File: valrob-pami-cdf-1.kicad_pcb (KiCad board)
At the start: 4 copper layers, 58 x 50 mm, 138 parts, among them J1 Conn_01x04, J2 USB_C_Receptacle_USB2.0_14P, J3 Conn_01x02, J4 Conn_01x04_Pin, J5 Conn_01x06, M1 Motor_Servo, M2 Stepper_Motor_bipolar, M3 Stepper_Motor_bipolar, Q1 Q_NMOS, Q2 Q_NMOS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

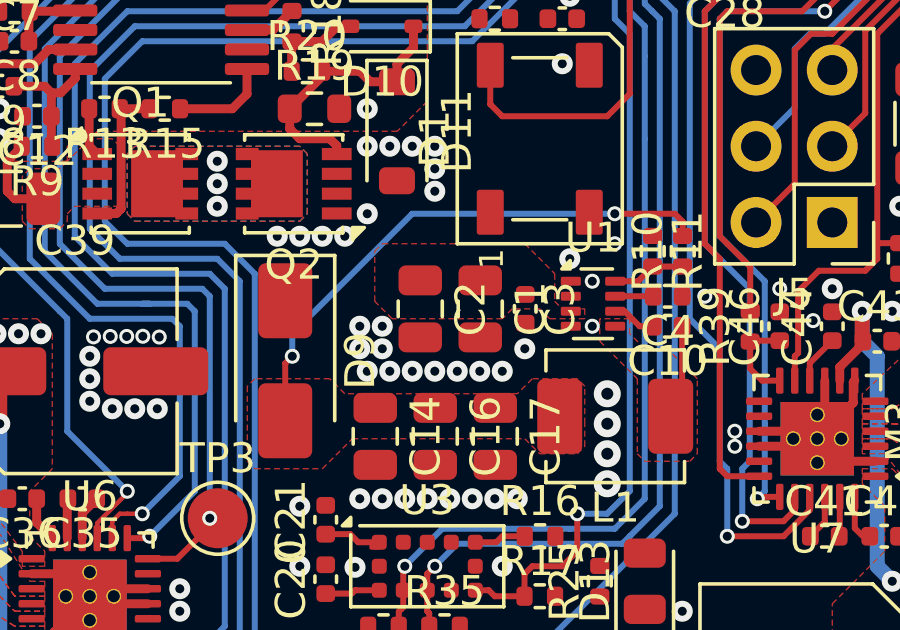
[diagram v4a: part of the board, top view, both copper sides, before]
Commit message: pcb: add +BATT routing
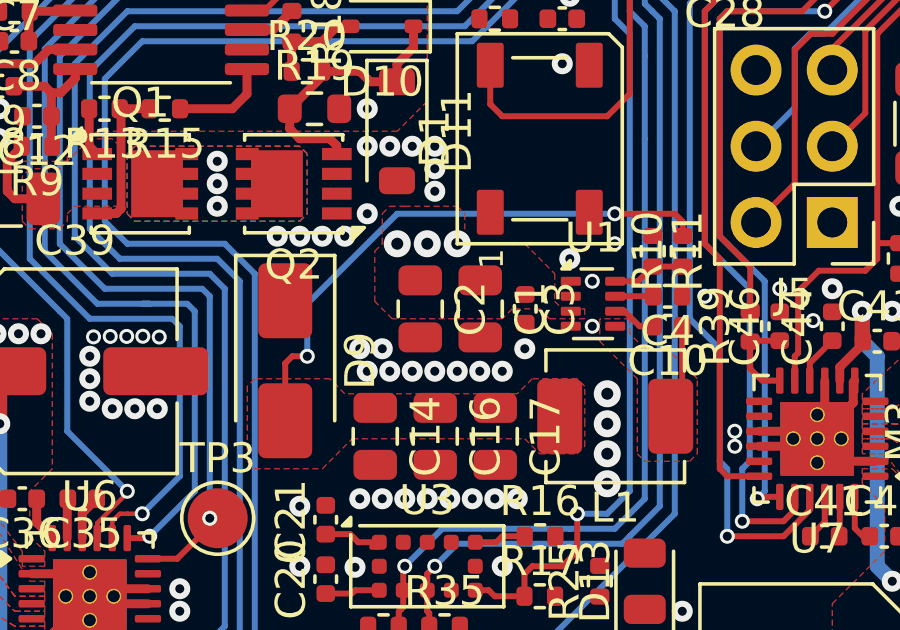
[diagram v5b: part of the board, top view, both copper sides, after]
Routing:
- net +BATT: track 55.5 -> 140.5 mm, vias 14 -> 17
- net +5V: track 18.3 -> 18.9 mm
- net GND: vias 113 -> 111
- added copper zone on In2.Cu, net +BATT
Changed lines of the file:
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@@
 	)
 	(via
-		(at 153.25 105.75)
-		(size 0.7)
-		(drill 0.3)
-		(layers "F.Cu" "B.Cu")
-		(free yes)
-		(net 4)
-	)
-	(via
 		(at 155.75 101.25)
 		(size 0.7)
@@
 	)
 	(via
-		(at 154 105.75)
-		(size 0.7)
-		(drill 0.3)
-		(layers "F.Cu" "B.Cu")
-		(free yes)
-		(net 4)
-	)
-	(via
 		(at 146.5 108.5)
 		(size 0.7)
@@
 	)
 	(via
+		(at 154.5 103)
+		(size 0.9)
+		(drill 0.4)
+		(layers "F.Cu" "B.Cu")
+		(free yes)
+		(net 5)
+	)
+	(via
 		(at 169.939328 119.069201)
 		(size 0.7)
@@
 	)
 	(via
+		(at 155.5 103)
+		(size 0.9)
+		(drill 0.4)
+		(layers "F.Cu" "B.Cu")
+		(free yes)
+		(net 5)
+	)
+	(via
+		(at 156.5 103)
+		(size 0.9)
+		(drill 0.4)
+		(layers "F.Cu" "B.Cu")
+		(free yes)
+		(net 5)
+	)
+	(via
 		(at 139.624264 106)
 		(size 0.7)
@@
 	)
 	(segment
+		(start 149.749 106.249)
+		(end 149.749 114.371735)
+		(width 2)
+		(layer "In2.Cu")
+		(net 5)
+	)
+	(segment
+		(start 149.749 114.371735)
+		(end 150.877265 115.5)
+		(width 2)
+		(layer "In2.Cu")
+		(net 5)
+	)
+	(segment
+		(start 151.25 115.5)
+		(end 156.75 121)
+		(width 2)
+		(layer "In2.Cu")
+		(net 5)
+	)
+	(segment
+		(start 156.75 121)
+		(end 168.758529 121)
+		(width 2)
+		(layer "In2.Cu")
+		(net 5)
+	)
+	(segment
+		(start 141.124264 106)
+		(end 143.374264 103.75)
+		(width 2)
+		(layer "In2.Cu")
+		(net 5)
+	)
+	(segment
+		(start 131 100.5)
+		(end 133.25 102.75)
+		(width 3)
+		(layer "In2.Cu")
+		(net 5)
+	)
+	(segment
+		(start 147.25 103.75)
+		(end 149.749 106.249)
+		(width 2)
+		(layer "In2.Cu")
+		(net 5)
+	)
+	(segment
+		(start 168.758529 121)
+		(end 170.689328 119.069201)
+		(width 2)
+		(layer "In2.Cu")
+		(net 5)
+	)
+	(segment
+		(start 141.515 85.575)
+		(end 138.59 88.5)
+		(width 3)
+		(layer "In2.Cu")
+		(net 5)
+	)
+	(segment
+		(start 138.59 88.5)
+		(end 133.5 88.5)
+		(width 3)
+		(layer "In2.Cu")
+		(net 5)
+	)
+	(segment
+		(start 133.25 102.75)
+		(end 137.874264 102.75)
+		(width 3)
+		(layer "In2.Cu")
+		(net 5)
+	)
+	(segment
+		(start 149.749 106.249)
+		(end 151.498 104.5)
+		(width 2)
+		(layer "In2.Cu")
+		(net 5)
+	)
+	(segment
+		(start 150.877265 115.5)
+		(end 151.25 115.5)
+		(width 2)
+		(layer "In2.Cu")
+		(net 5)
+	)
+	(segment
+		(start 151.498 104.5)
+		(end 154 104.5)
+		(width 2)
+		(layer "In2.Cu")
+		(net 5)
+	)
+	(segment
+		(start 154 104.5)
+		(end 155.5 103)
+		(width 2)
+		(layer "In2.Cu")
+		(net 5)
+	)
+	(segment
+		(start 137.874264 102.75)
+		(end 141.124264 106)
+		(width 3)
+		(layer "In2.Cu")
+		(net 5)
+	)
+	(segment
+		(start 131 91)
+		(end 131 100.5)
+		(width 3)
+		(layer "In2.Cu")
+		(net 5)
+	)
+	(segment
+		(start 143.374264 103.75)
+		(end 147.25 103.75)
+		(width 2)
+		(layer "In2.Cu")
+		(net 5)
+	)
+	(segment
+		(start 133.5 88.5)
+		(end 131 91)
+		(width 3)
+		(layer "In2.Cu")
+		(net 5)
+	)
+	(segment
 		(start 163.035 104.75)
 		(end 161.765 104.75)
@@
 	)
 	(segment
-		(start 150.765 106.985)
-		(end 151 106.75)
-		(width 0.2)
-		(layer "F.Cu")
-		(net 17)
-	)
-	(segment
 		(start 164.015 102.74)
 		(end 164.015 102.76)
@@
 	)
 	(segment
-		(start 150.765 108.9)
+		(start 151 106.75)
 		(end 150.765 106.985)
 		(width 0.2)
@@
 	)
 	(segment
+		(start 150.765 106.985)
+		(end 150.765 108.9)
+		(width 0.2)
+		(layer "F.Cu")
+		(net 17)
+	)
+	(segment
+		(start 151.5 106.75)
+		(end 151 106.75)
+		(width 0.2)
+		(layer "F.Cu")
+		(net 17)
+	)
+	(segment
 		(start 163.75 102)
 		(end 164.015 102.265)
@@
 	)
 	(via
-		(at 151 106.75)
+		(at 151.5 106.75)
 		(size 0.5)
 		(drill 0.3)
@@
 	)
 	(segment
-		(start 151 106)
-		(end 151 106.75)
+		(start 151.5 106.75)
+		(end 151.5 105)
 		(width 0.2)
 		(layer "B.Cu")
@@
 	)
 	(segment
-		(start 161.75 102)
-		(end 155 102)
+		(start 154.5 102)
+		(end 161.75 102)
 		(width 0.2)
 		(layer "B.Cu")
@@
 	)
 	(segment
-		(start 155 102)
-		(end 151 106)
+		(start 151.5 105)
+		(end 154.5 102)
 		(width 0.2)
 		(layer "B.Cu")
@@
 			(pts
 				(xy 160.75 105.5) (xy 159.58 105.5) (xy 159.25 105.17) (xy 158.33 105.17) (xy 158 105.5) (xy 154.33 105.5)
-				(xy 153.75 104.92) (xy 153.75 103.25) (xy 154 103) (xy 158.75 103) (xy 159.75 104) (xy 159.75 104.92)
-				(xy 160 105.17) (xy 160.75 105.17)
+				(xy 153.75 104.92) (xy 153.75 103.25) (xy 154 103) (xy 154 102) (xy 154.25 101.75) (xy 154.75 101.75)
+				(xy 156.5 101.75) (xy 156.75 102) (xy 156.75 102.75) (xy 157 103) (xy 158.75 103) (xy 159.75 104)
+				(xy 159.75 104.92) (xy 160 105.17) (xy 160.75 105.17)
 			)
 		)
@@
 			)
 		)
+	)
+	(zone
+		(net 5)
+		(net_name "+BATT")
+		(layer "In2.Cu")
+		(hatch edge 0.5)
+		(priority 15)
+		(connect_pads yes
+			(clearance 0.2)
+		)
+		(min_thickness 0.15)
+		(filled_areas_thickness no)
+		(fill yes
+			(thermal_gap 0.25)
+			(thermal_bridge_width 0.35)
+		)
+		(polygon
+			(pts
+				(xy 169 119.5) (xy 168.75 119.25) (xy 168.75 118.75) (xy 169 118.5) (xy 172.5 118.5) (xy 172.75 118.75)
+				(xy 172.75 119.25) (xy 172.5 119.5)
+			)
+		)
+	)
+	(zone
+		(net 5)
+		(net_name "+BATT")
+		(layer "In2.Cu")
+		(hatch edge 0.5)
+		(priority 16)
+		(connect_pads yes
+			(clearance 0.2)
+		)
+		(min_thickness 0.15)
+		(filled_areas_thickness no)
+		(fill yes
+			(thermal_gap 0.25)
+			(thermal_bridge_width 0.35)
+		)
+		(polygon
+			(pts
+				(xy 156.5 103.75) (xy 157 103.25) (xy 157 102.25) (xy 156.5 101.75) (xy 154.5 101.75) (xy 154 102.25)
+				(xy 154 103.25) (xy 154.5 103.75)
+			)
+		)

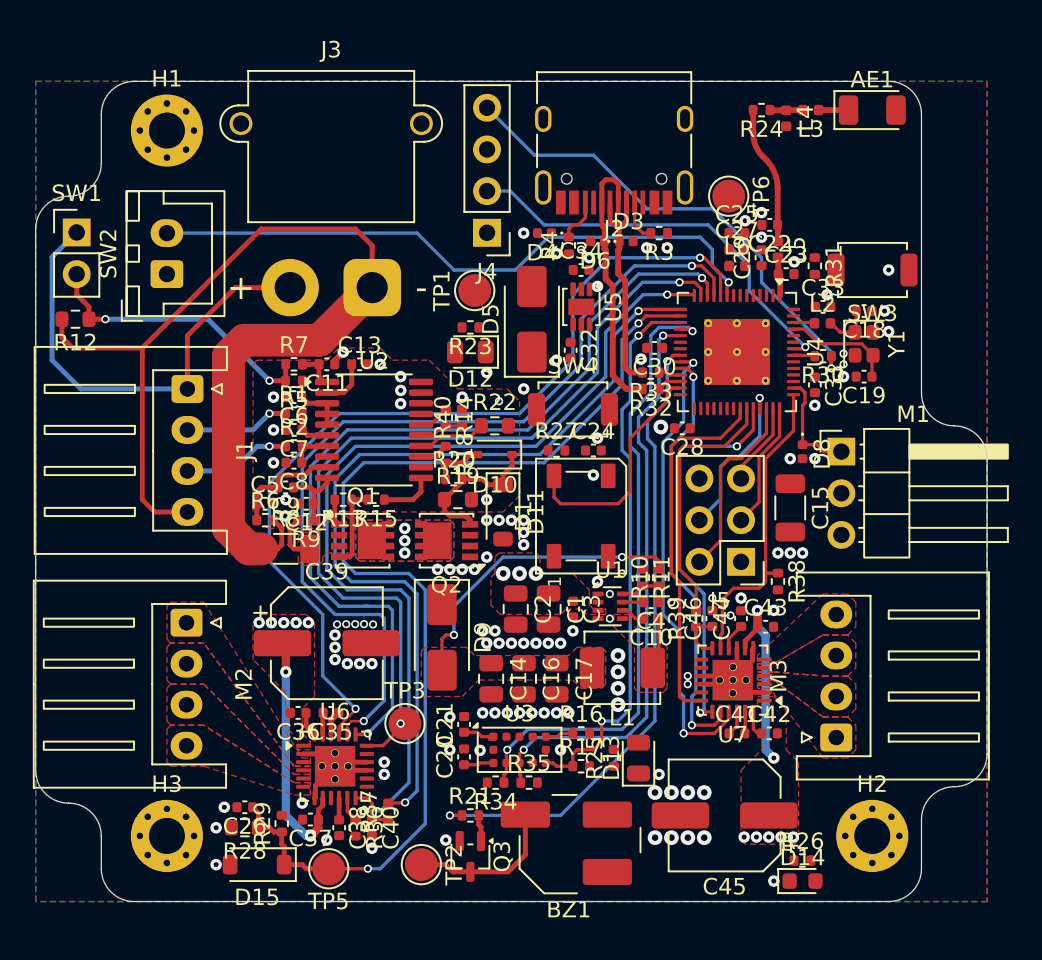
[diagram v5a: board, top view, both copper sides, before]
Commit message: pcb: add +3V3 pwr routing
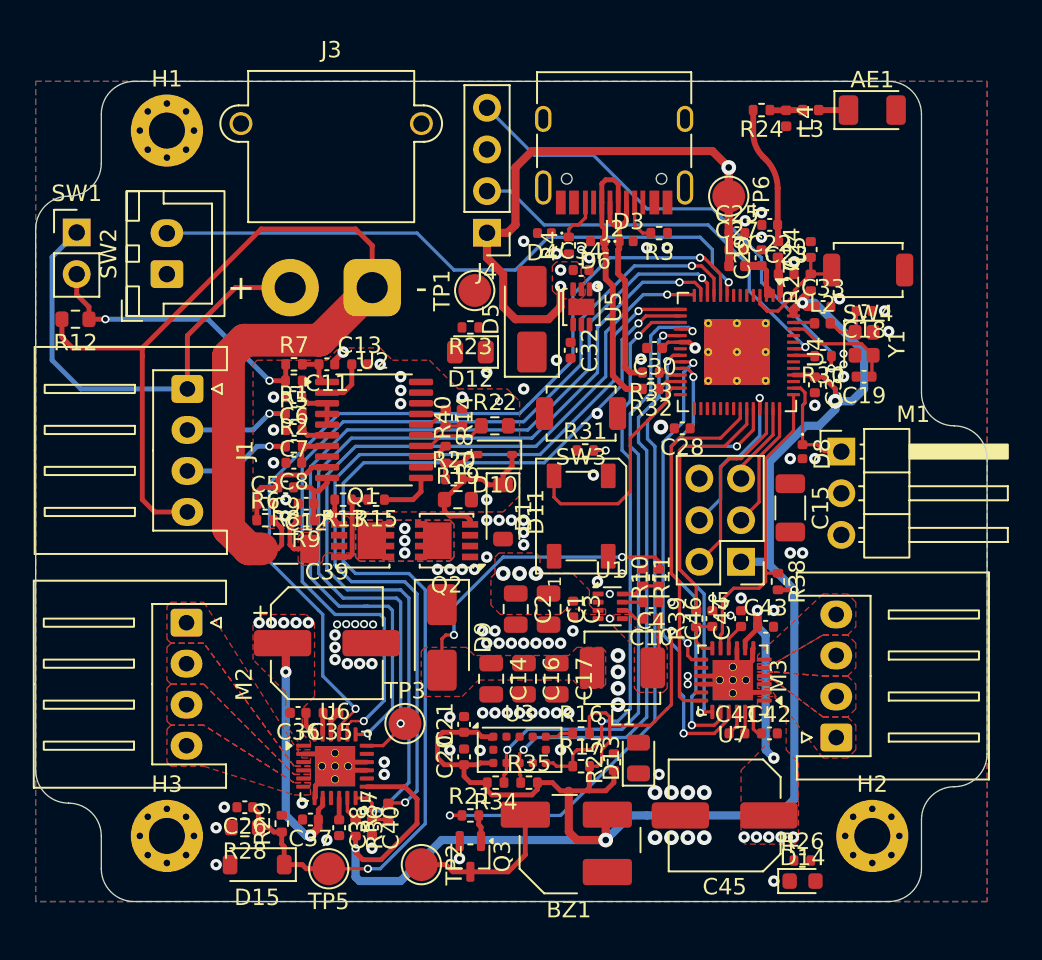
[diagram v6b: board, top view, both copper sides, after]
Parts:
- moved SW4 19.9 mm to (176.8, 84.5), turned to 180 degrees
- moved SW3 19.8 mm to (159.2, 93.2)
- moved R27 18.6 mm to (173.2, 85.2), turned to 90 degrees
- moved C24 18.0 mm to (173.2, 83.2), turned to 90 degrees
- moved R31 18.0 mm to (159.5, 95.5), turned to 0 degrees
- moved R25 0.25 mm to (161.2, 114.5)
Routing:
- net +3V3: track 3.73 -> 200.2 mm, vias 0 -> 12
- net /CHIP_PU: track 0.00 -> 7.10 mm
- net VDD3P3: track 0.00 -> 4.01 mm
- net GND: vias 111 -> 109
- added copper zone on F.Cu, net +3V3

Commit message: pcb: add 5V pwr routing
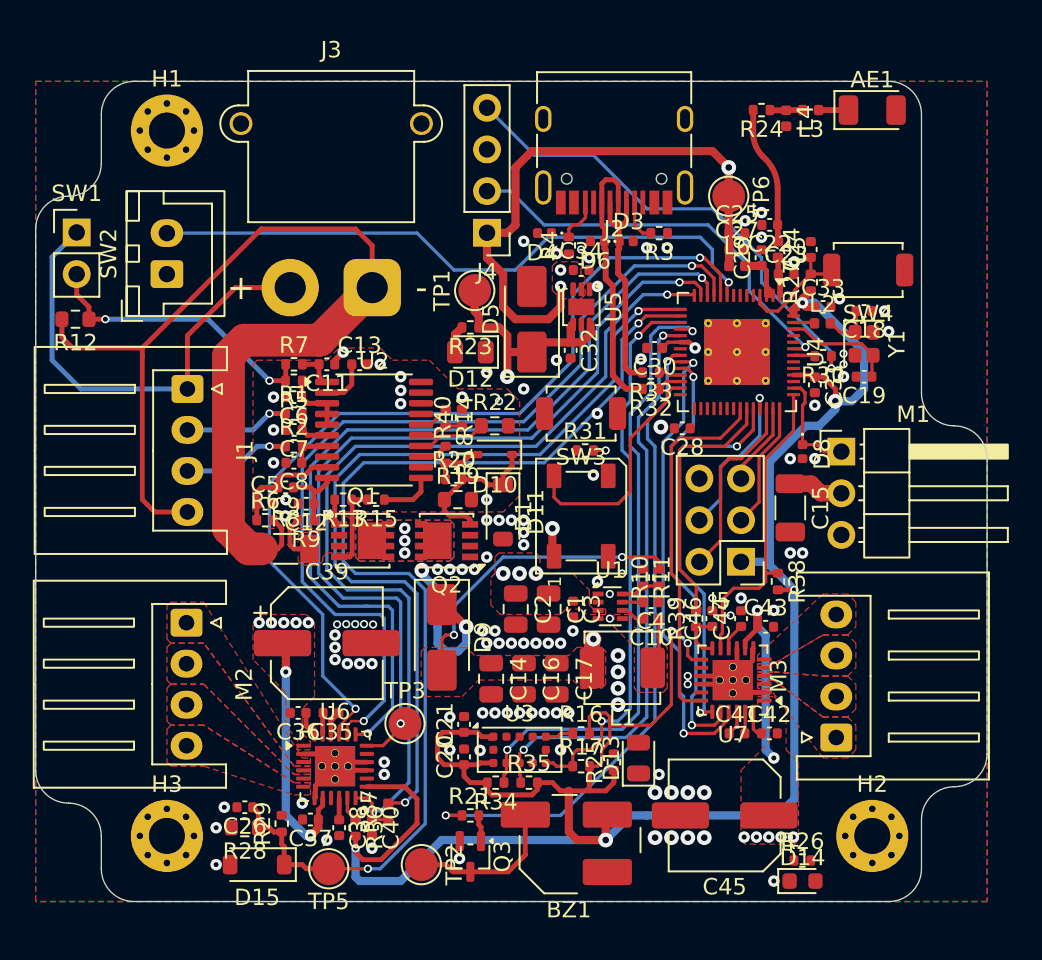
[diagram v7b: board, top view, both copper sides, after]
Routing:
- net +5V_MCU: track 0.00 -> 45.5 mm, vias 0 -> 4
- net +5V: track 18.9 -> 46.5 mm, vias 2 -> 3
- net Net-(D12-A): track 0.00 -> 1.68 mm
- net /BUZZER: track 39.2 -> 39.7 mm

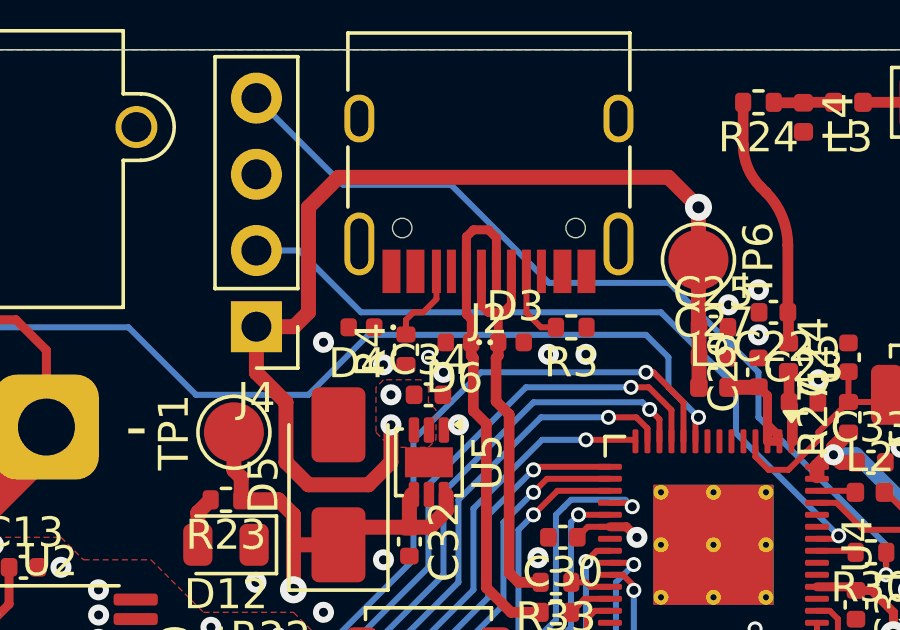
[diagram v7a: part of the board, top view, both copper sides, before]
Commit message: pcb: add +VBUS pwr routing
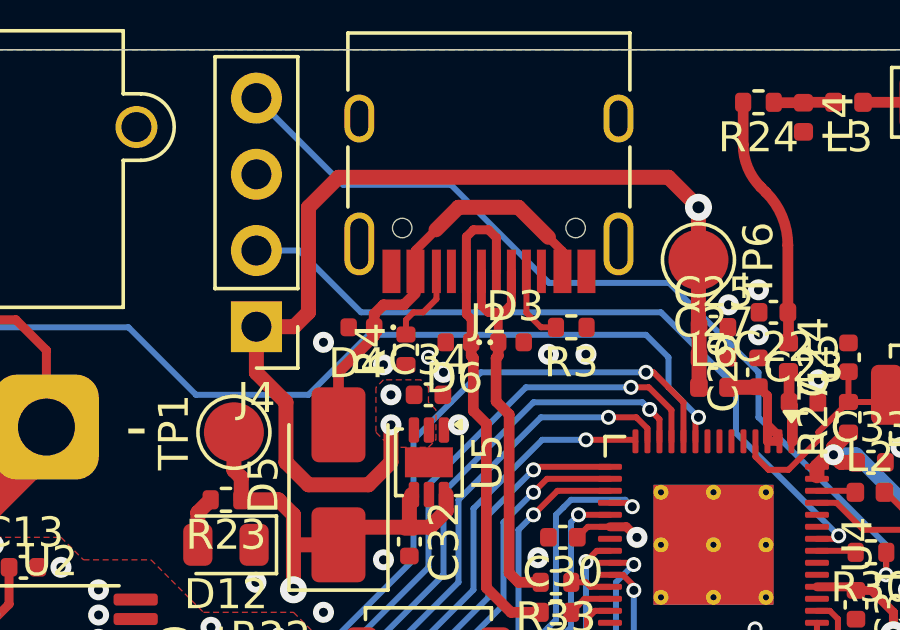
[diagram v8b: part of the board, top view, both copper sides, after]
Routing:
- net +Vbus: track 0.00 -> 14.0 mm
